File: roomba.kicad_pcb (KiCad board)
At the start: 2 copper layers, 26.7 x 38.1 mm, 13 parts, among them J1 Conn_01x07_Male, U1 TSR_1-2450, U2 NCP1117-3.3_SOT223, U3 TXB0104D, U4 ESP-12F

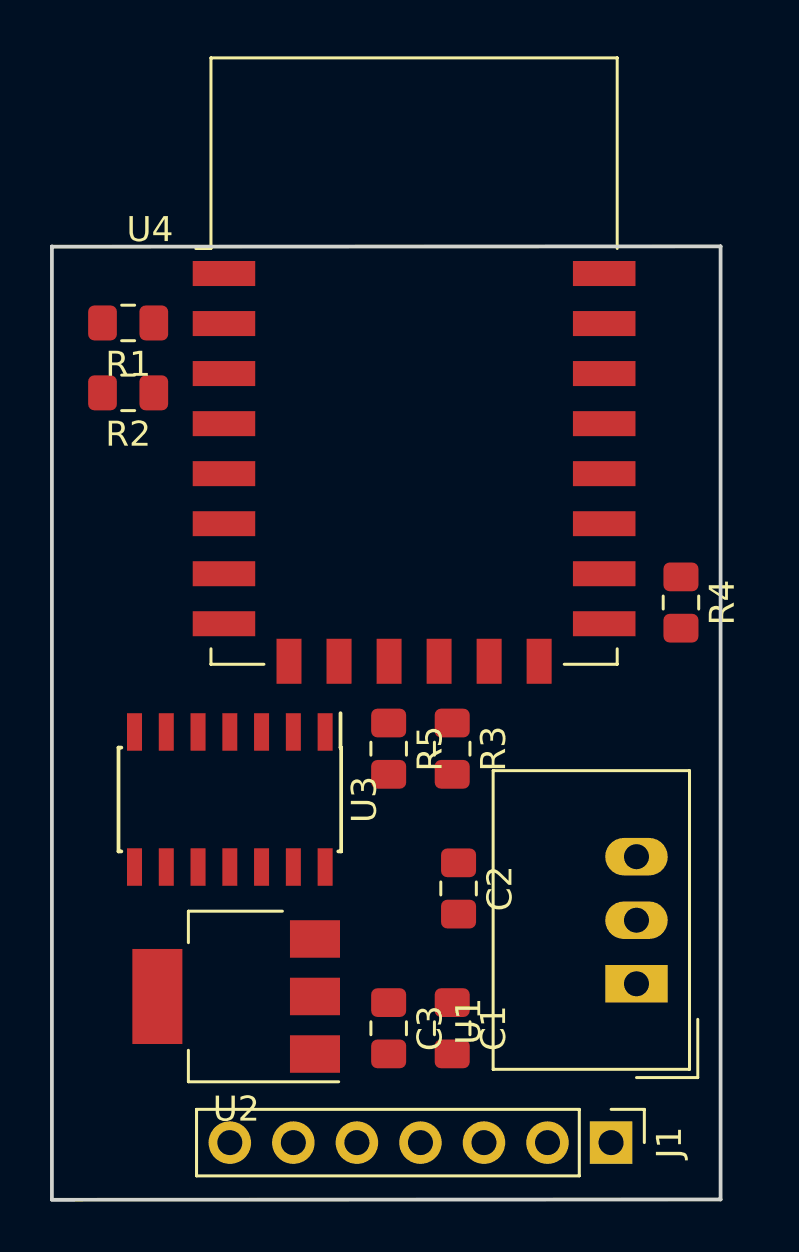
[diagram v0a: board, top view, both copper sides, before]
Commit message: Routed PCB for Roomba
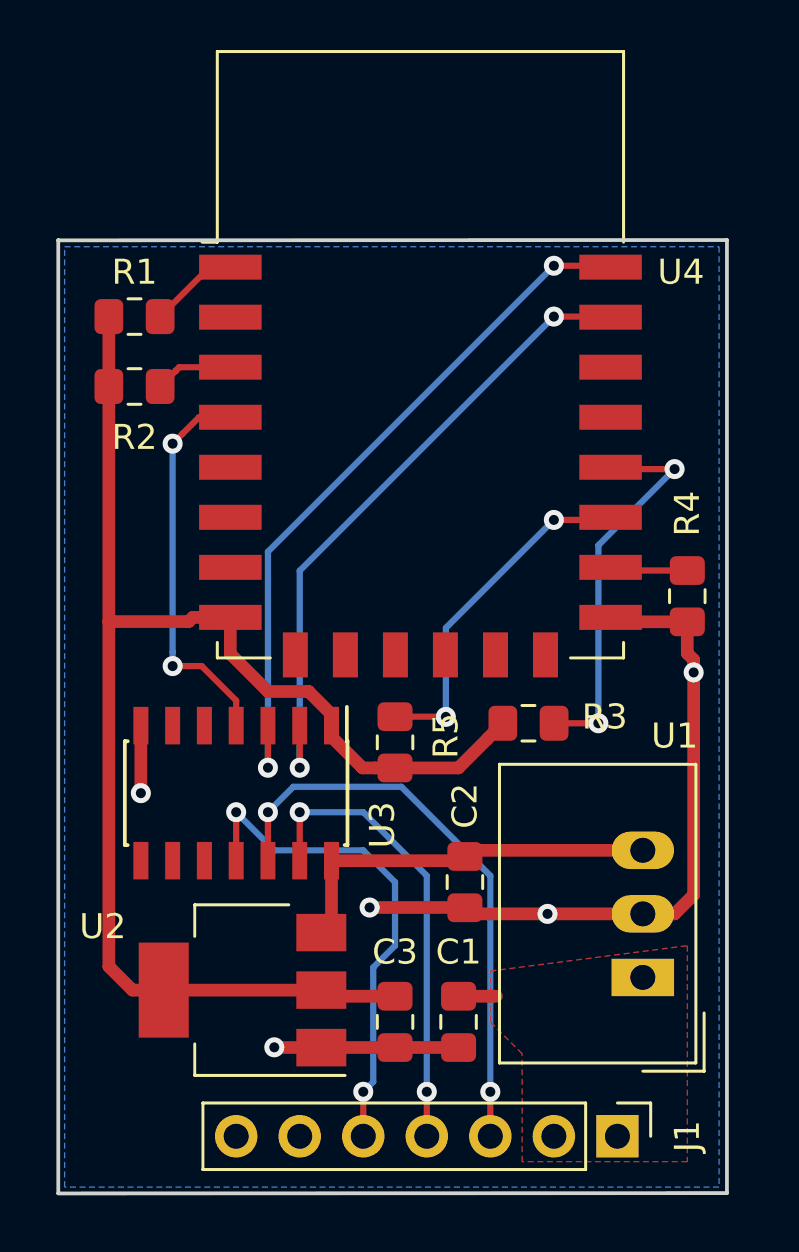
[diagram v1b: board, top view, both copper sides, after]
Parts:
- moved R3 3.21 mm to (148.3, 98.0), turned to 180 degrees
- moved C3 0.36 mm to (143.0, 110.0)
- moved R4 0.36 mm to (154.7, 93.0)
- moved R5 0.36 mm to (143.0, 98.8)
- moved U2 0.36 mm to (136.9, 108.7)
- moved C1 0.36 mm to (145.5, 110.0)
- moved J1 0.36 mm to (151.9, 114.6)
- moved R1 0.36 mm to (132.6, 81.8)
- moved R2 0.36 mm to (132.6, 84.6)
- moved U1 0.36 mm to (152.9, 108.2)
- moved U3 0.36 mm to (136.7, 100.8)
- moved U4 0.36 mm to (144.0, 83.3)
- moved C2 0.36 mm to (145.8, 104.4)
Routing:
- net +3V3: track 0.00 -> 59.1 mm
- net Earth: track 0.00 -> 37.6 mm, vias 0 -> 5
- net /LOCAL_TXD: track 0.00 -> 28.8 mm, vias 0 -> 2
- net /LOCAL_RXD: track 0.00 -> 26.2 mm, vias 0 -> 2
- net /ROOMBA_RXD: track 0.00 -> 23.1 mm, vias 0 -> 2
- net /ROOMBA_BRC: track 0.00 -> 20.1 mm, vias 0 -> 2
- net /ROOMBA_TXD: track 0.00 -> 18.5 mm, vias 0 -> 2
- net /GPIO0: track 0.00 -> 15.8 mm, vias 0 -> 2
- net /LOCAL_BRC: track 0.00 -> 15.7 mm, vias 0 -> 2
- net +5V: track 0.00 -> 15.7 mm
- net /GPIO2: track 0.00 -> 14.0 mm, vias 0 -> 2
- net Net-(R1-Pad1): track 0.00 -> 3.62 mm
- net Net-(R2-Pad1): track 0.00 -> 3.13 mm
- net Net-(R4-Pad1): track 0.00 -> 3.12 mm
- net +BATT: track 0.00 -> 1.51 mm
- added copper zone on F.Cu, net +BATT
- added copper zone on B.Cu, net Earth
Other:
- net class Power added: clearance 0.2, trace_width 0.508, via_dia 0.8, via_drill 0.4

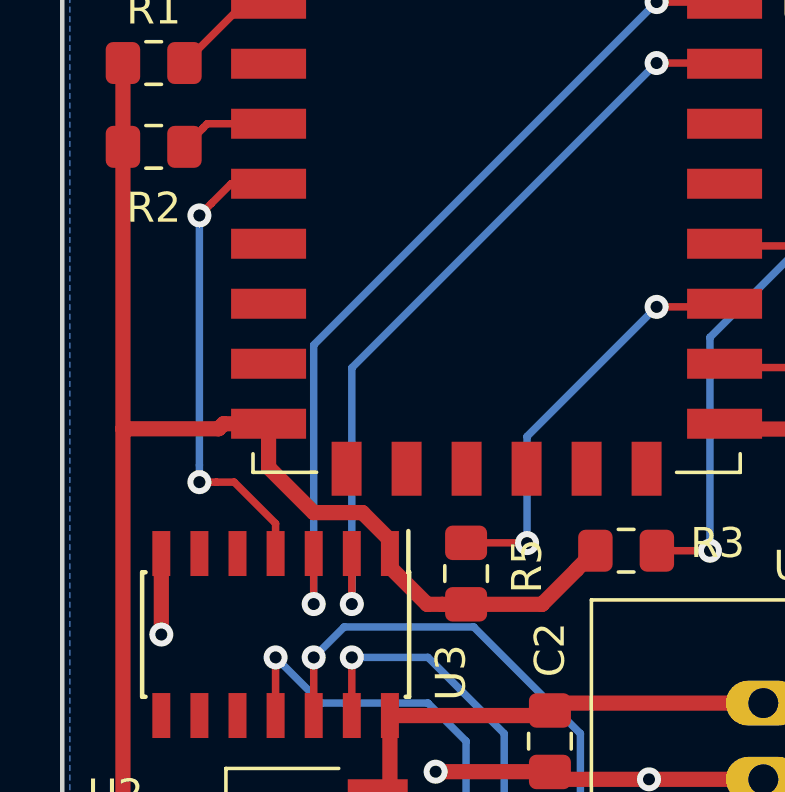
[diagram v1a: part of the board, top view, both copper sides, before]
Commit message: Adding silkscreen and title/date information.
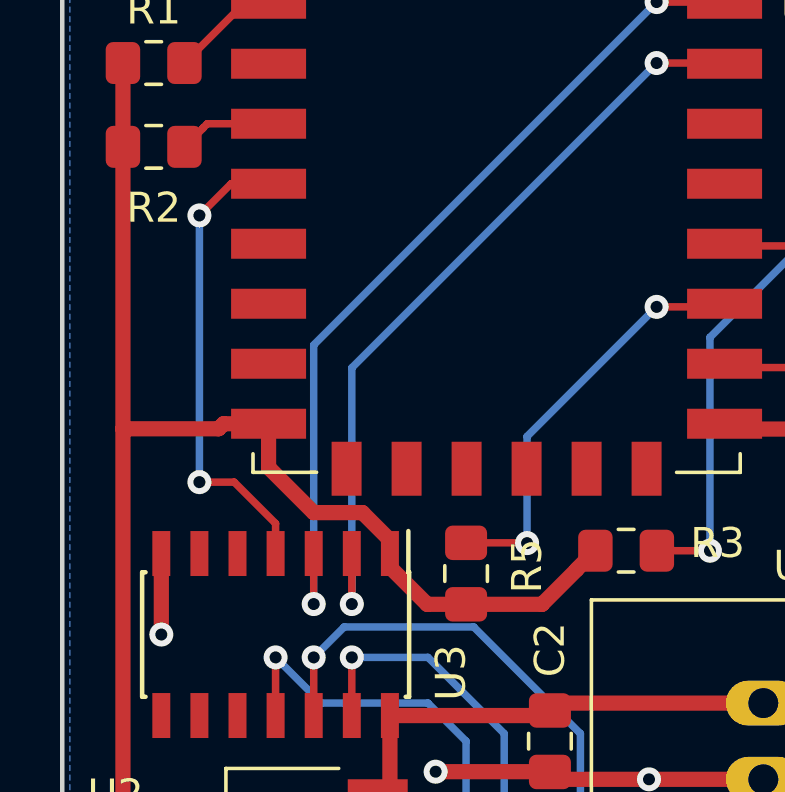
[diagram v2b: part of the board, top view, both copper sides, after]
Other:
- board text added: "Roomba 560 ESP-Wifi Rev -- Matthew A Sparks"

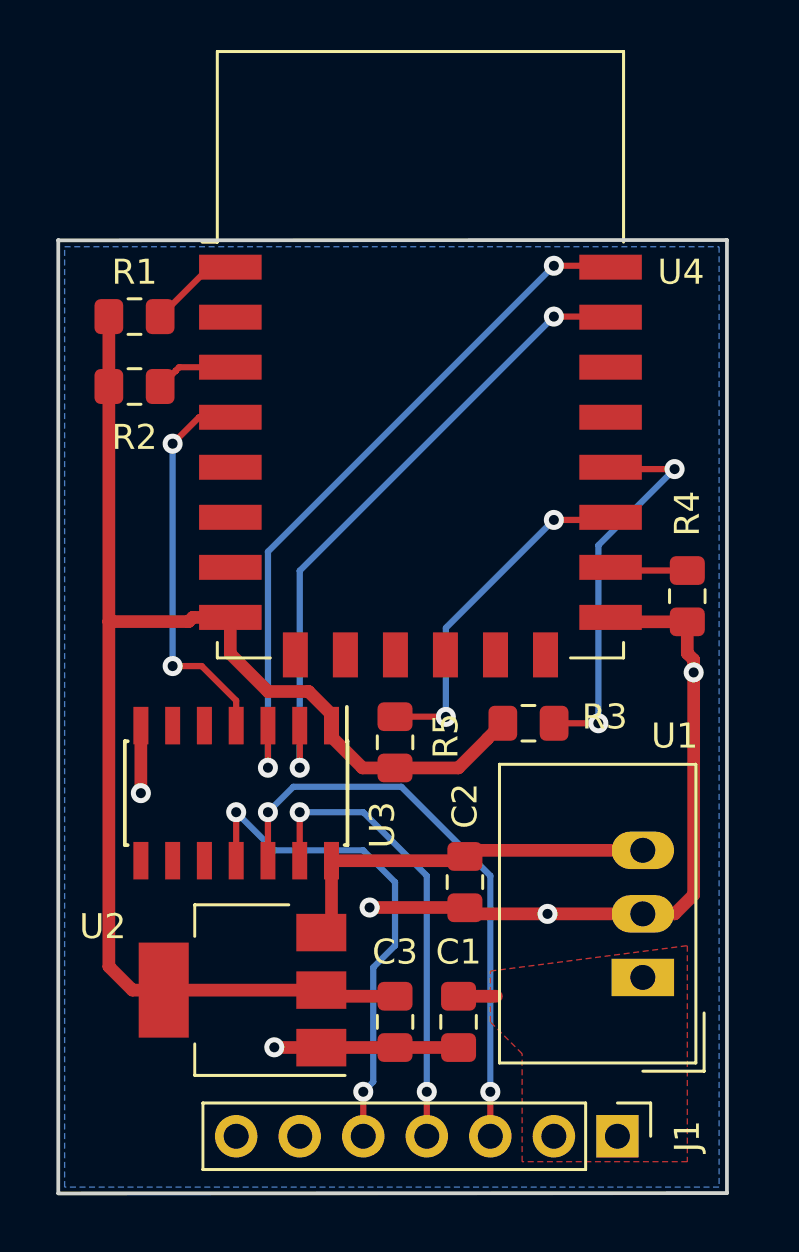
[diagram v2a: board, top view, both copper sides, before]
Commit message: Updated layout to a 1 by 1.2 inch size. Components are now on both sides. Solder Mask Clearance adjusted to 0.002in
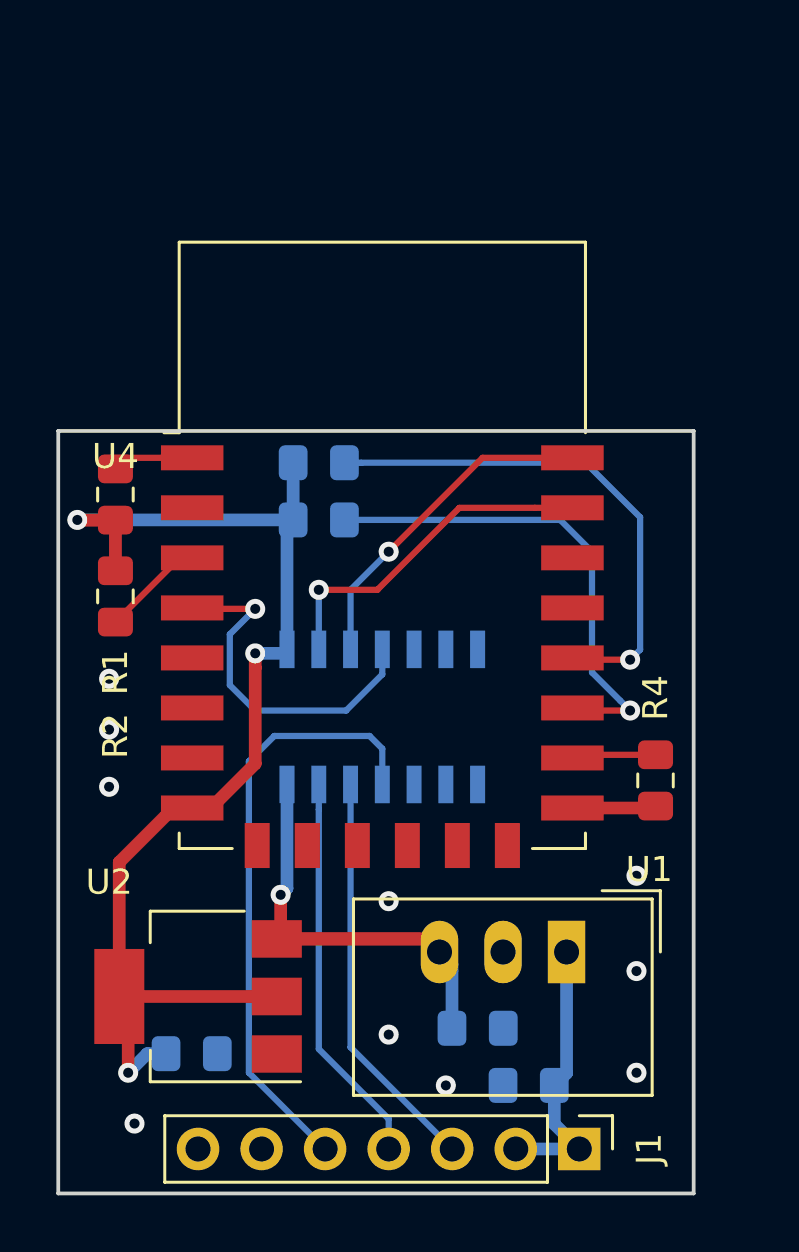
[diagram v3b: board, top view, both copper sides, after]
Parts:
- C1, C2, C3, R3, R5, U3: moved to B.Cu
- moved R3 13.4 mm to (140.0, 87.6)
- moved R5 9.40 mm to (140.0, 89.9), turned to 180 degrees
- moved R2 8.43 mm to (131.8, 93.0), turned to 90 degrees
- moved C3 8.23 mm to (134.9, 111.3), turned to 0 degrees
- moved U4 7.77 mm to (142.5, 90.9)
- moved R4 7.47 mm to (153.4, 100.3)
- moved R1 7.15 mm to (131.8, 88.9), turned to 270 degrees
- moved U3 6.59 mm to (142.5, 97.8)
- moved C2 5.86 mm to (146.3, 110.2), turned to 0 degrees
- moved C1 3.78 mm to (148.3, 112.5), turned to 180 degrees
- moved U1 3.21 mm to (149.9, 107.2), turned to 180 degrees
- moved U2 1.80 mm to (135.1, 109.0)
- moved J1 1.61 mm to (150.4, 115.1)
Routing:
- net Earth: track 37.6 -> 3.35 mm, vias 5 -> 10
- net /LOCAL_TXD: track 28.8 -> 13.4 mm, vias 2 -> 1
- net /LOCAL_RXD: track 26.2 -> 13.9 mm, vias 2 -> 1
- net +3V3: track 59.1 -> 48.7 mm, vias 0 -> 3
- net +BATT: track 1.51 -> 11.0 mm
- net +5V: track 15.7 -> 22.7 mm, vias 0 -> 1
- net /ROOMBA_RXD: track 23.1 -> 16.3 mm, vias 2 -> 0
- net /GPIO2: track 14.0 -> 19.8 mm, vias 2 -> 1
- net /GPIO0: track 15.8 -> 20.9 mm, vias 2 -> 1
- net /ROOMBA_BRC: track 20.1 -> 24.2 mm, vias 2 -> 0
- net /ROOMBA_TXD: track 18.5 -> 15.7 mm, vias 2 -> 0
- net /LOCAL_BRC: track 15.7 -> 14.1 mm, vias 2 -> 1
- net Net-(R2-Pad1): track 3.13 -> 4.13 mm
- added copper zone on F.Cu, net Earth
- removed copper zone on F.Cu, net +BATT
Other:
- board size 26.7 x 38.1 mm -> 25.4 x 30.5 mm
- rule pad_to_mask_clearance: 0.2 -> 0.0508
- board text added: "Roomba 560 ESP-Wifi Rev A Matthew A Sparks"
- board text removed: "Roomba 560 ESP-Wifi Rev -- Matthew A Sparks"

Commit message: Removed TXB0104, since it was garbling UART.  Instead added voltage divider on TXD from Roomba, and ran RXD and BRC to Roomba directly.
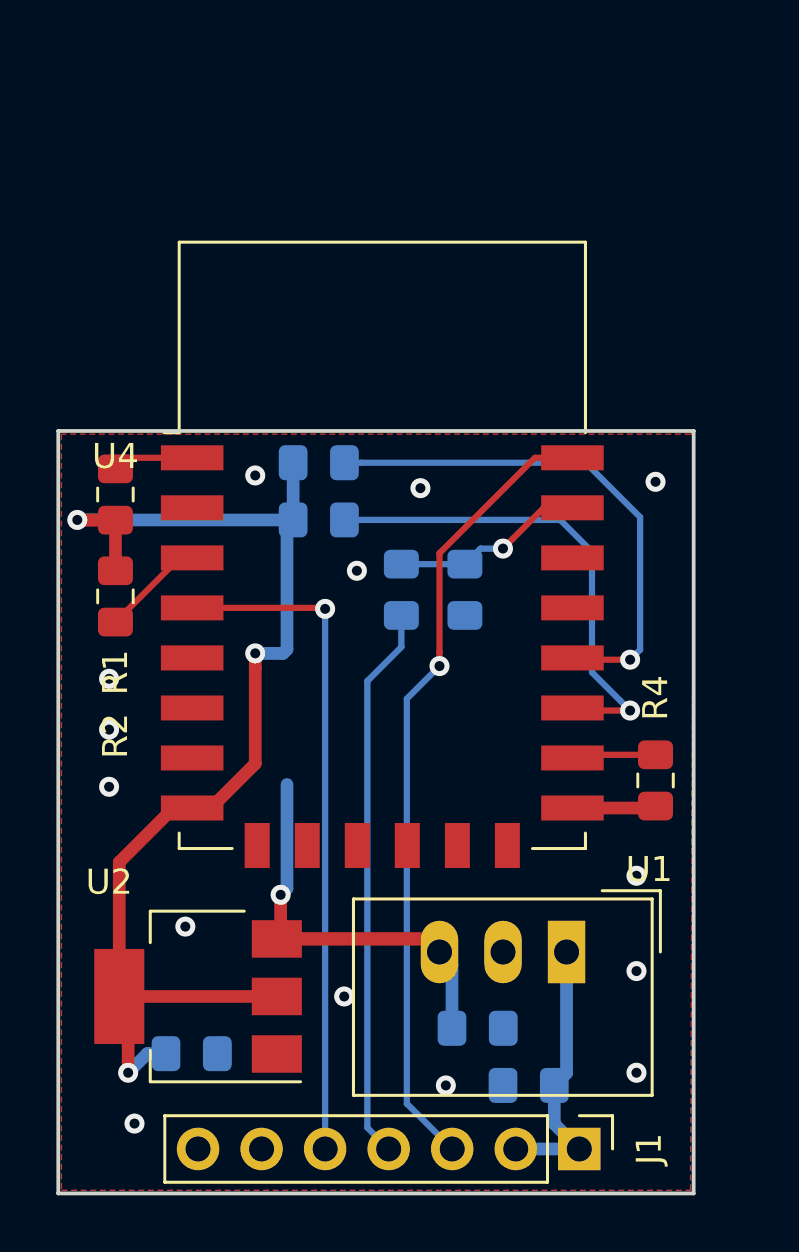
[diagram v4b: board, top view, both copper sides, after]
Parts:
- removed U3: TXB0104D, Package_SO:SOIC-14_3.9x8.7mm_P1.27mm
- added R6: 6.04K, Resistor_SMD:R_0805_2012Metric_Pad1.15x1.40mm_HandSolder, B.Cu at (143.3, 92.7)
- added R7: 12K, Resistor_SMD:R_0805_2012Metric_Pad1.15x1.40mm_HandSolder, B.Cu at (145.8, 92.7)
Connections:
- J1 pad 3: /ROOMBA_RXD -> /LOCAL_TXD
- J1 pad 5: /ROOMBA_BRC -> /LOCAL_BRC
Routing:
- net /ROOMBA_BRC: track 24.2 -> 0.00 mm
- net /LOCAL_TXD: track 13.4 -> 32.0 mm
- net /ROOMBA_RXD: track 16.3 -> 0.00 mm
- net /LOCAL_BRC: track 14.1 -> 27.0 mm
- net /ROOMBA_TXD: track 15.7 -> 22.2 mm
- net /LOCAL_RXD: track 13.9 -> 7.77 mm
- net +3V3: track 48.7 -> 49.2 mm
- net Earth: vias 10 -> 14

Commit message: Updating Roomba project to use buttons for reset/programming. Removing 5V to 3.3V translator in favor of voltage divider. Removing 5V to 3.3V regulator and going directly from BATT to 3.3V.
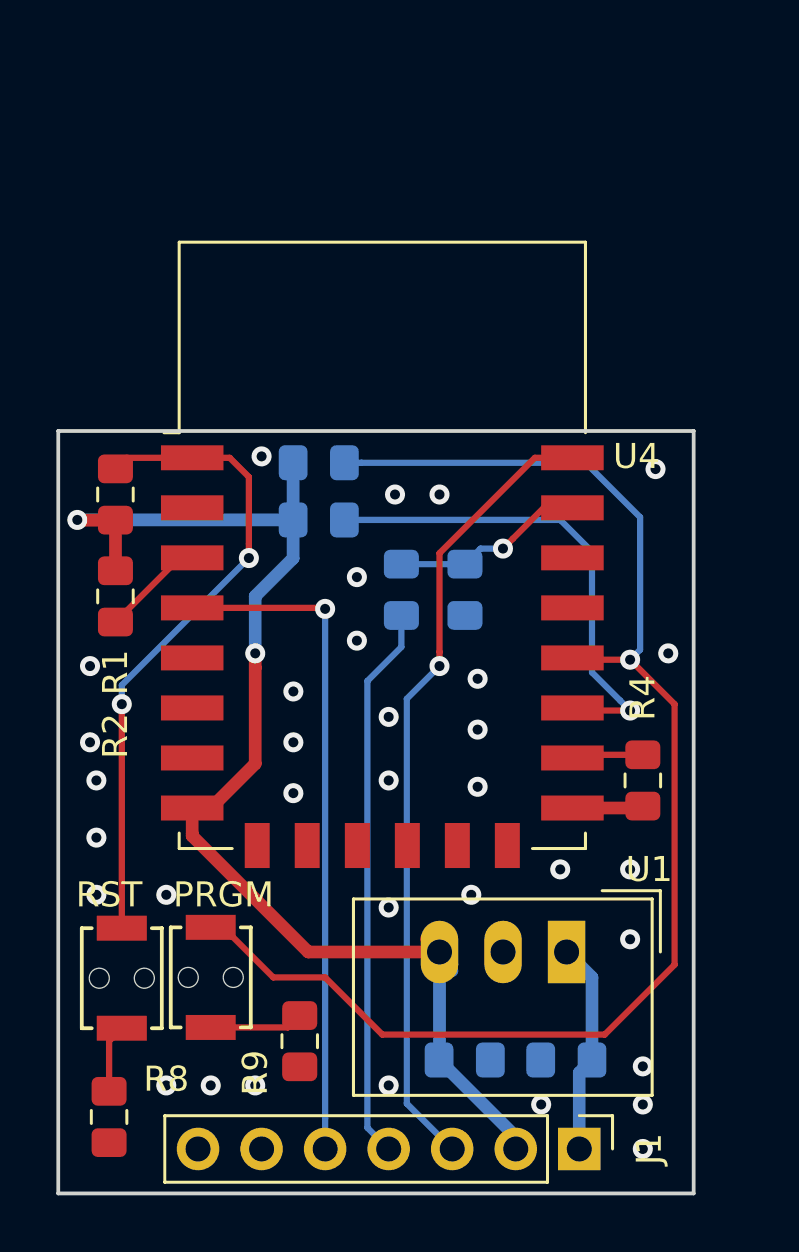
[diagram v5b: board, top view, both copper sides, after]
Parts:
- removed C2: 10 uF, Capacitor_SMD:C_0805_2012Metric_Pad1.15x1.40mm_HandSolder
- removed U2: NCP1117-3.3_SOT223, Package_TO_SOT_SMD:SOT-223-3_TabPin2
- added PRGM: SW_Push, pts820:PTS820, F.Cu at (135.6, 108.2)
- added R8: 470, Resistor_SMD:R_0805_2012Metric_Pad1.15x1.40mm_HandSolder, F.Cu at (131.6, 113.8)
- added R9: 470, Resistor_SMD:R_0805_2012Metric_Pad1.15x1.40mm_HandSolder, F.Cu at (139.2, 110.8)
- added RST: SW_Push, pts820:PTS820, F.Cu at (132.1, 108.2)
- U1: value TSR_1-2450 -> TSR_1-2433
- moved C3 10.9 mm to (145.8, 111.5)
- moved C1 1.82 mm to (149.9, 111.5)
- moved R4 0.51 mm to (152.9, 100.3)
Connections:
- J1 pad 2: +BATT -> +3V3
- U1 pad 3: +5V -> +3V3
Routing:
- net /GPIO0: track 20.9 -> 55.3 mm
- net +5V: track 22.7 -> 0.00 mm, vias 1 -> 0
- net Net-(R1-Pad1): track 3.25 -> 26.0 mm, vias 0 -> 2
- net +3V3: track 49.2 -> 53.4 mm, vias 3 -> 2
- net Net-(R9-Pad2): track 0.00 -> 3.75 mm
- net Net-(R8-Pad2): track 0.00 -> 2.73 mm
- net +BATT: track 11.0 -> 8.51 mm
- net Net-(R4-Pad1): track 3.37 -> 2.87 mm
- net Earth: track 3.35 -> 2.85 mm, vias 14 -> 34
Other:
- board text added: "Roomba 560 ESP-Wifi Rev B Matthew A Sparks"
- board text removed: "Roomba 560 ESP-Wifi Rev A Matthew A Sparks"
